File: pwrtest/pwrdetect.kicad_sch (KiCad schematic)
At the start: 37 parts, among them Q2 BC847, Q3 BC847, Q4 BC847, Q5 BC847, Q6 BC857, U10 TL431, U6 TL431DBZ, U7 TL431DBZ, U8 TL431DBZ, U9 TL431

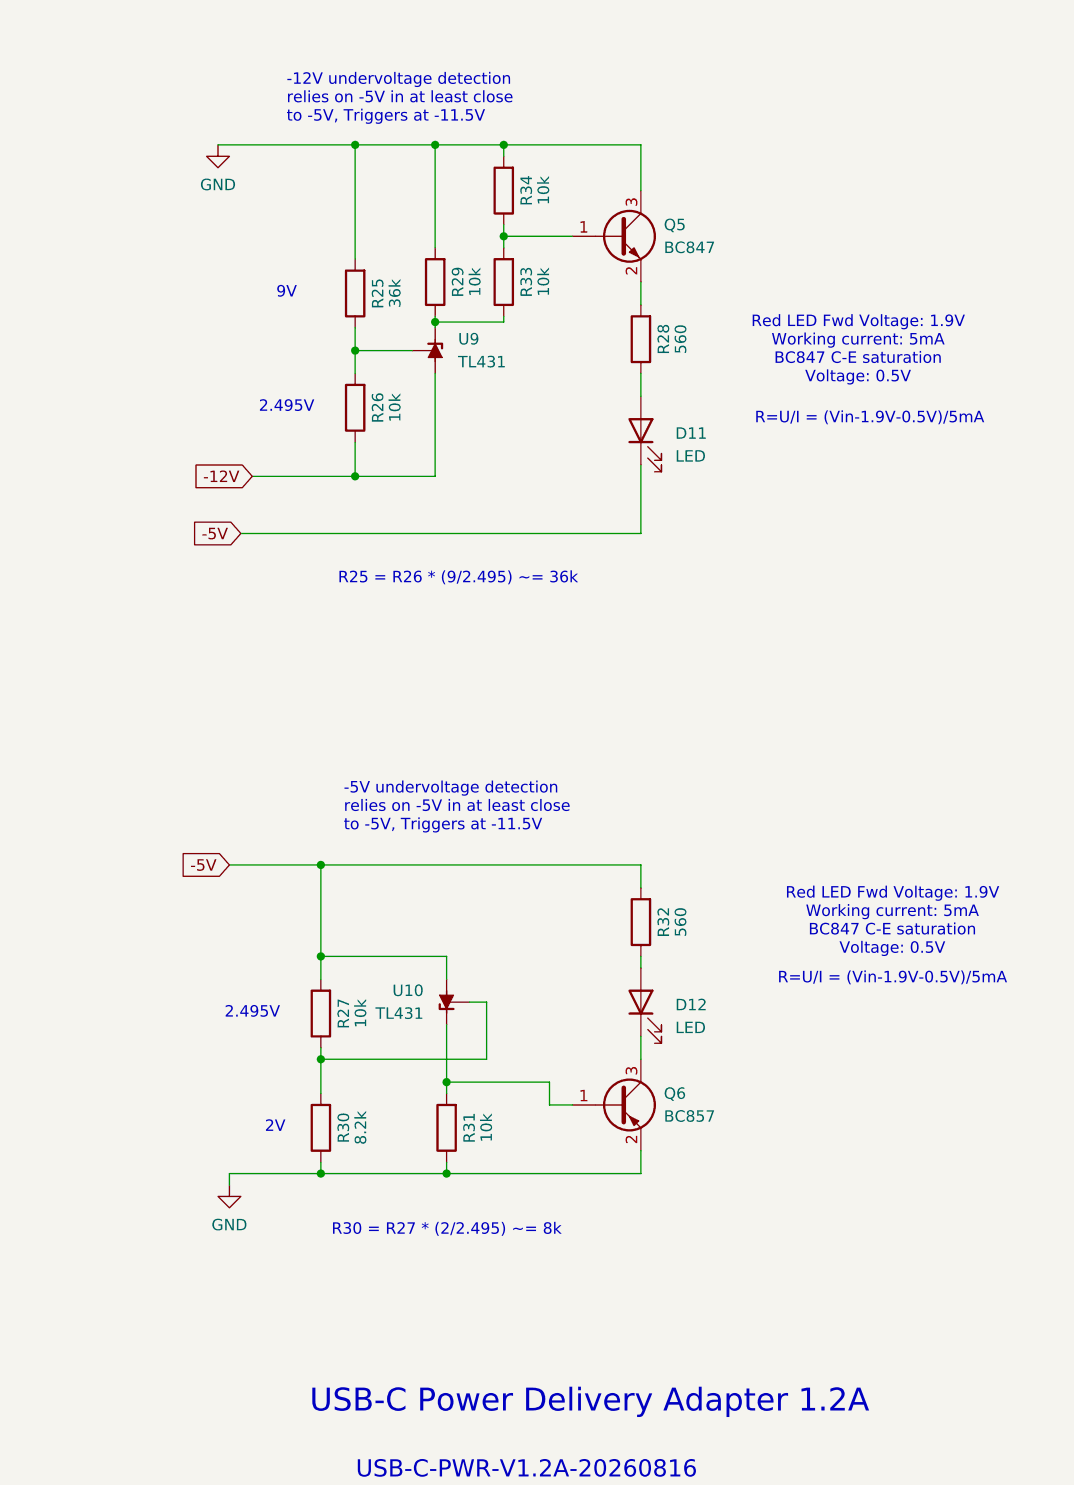
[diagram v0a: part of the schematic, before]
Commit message: new pwr adapter layout
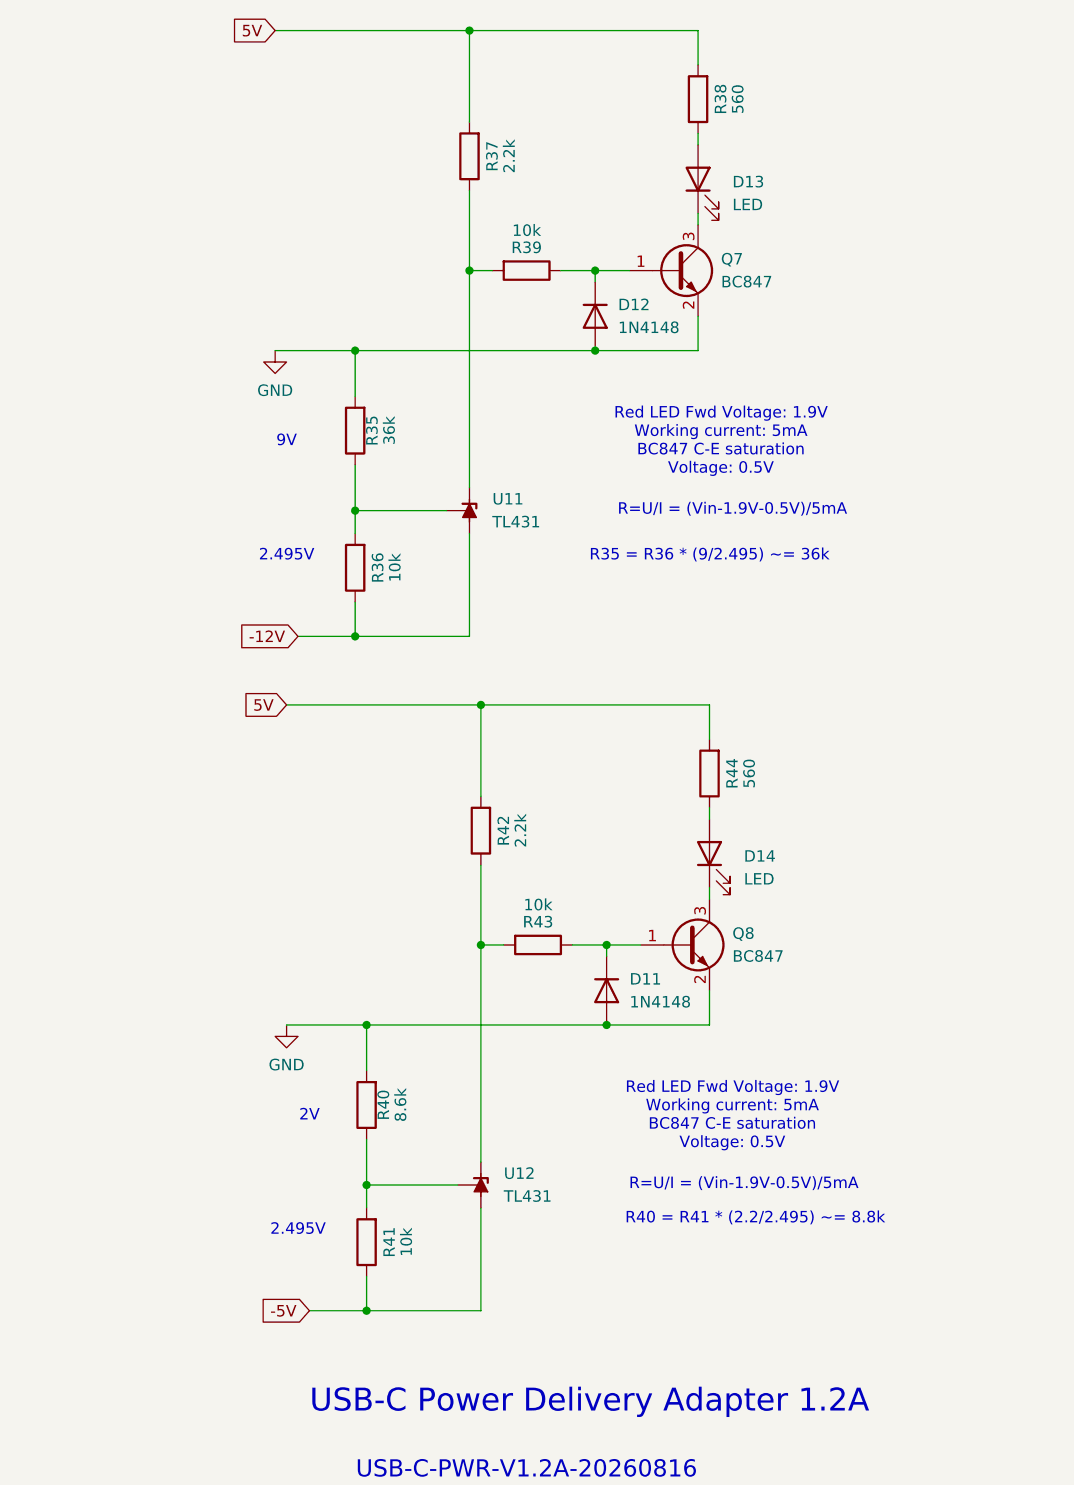
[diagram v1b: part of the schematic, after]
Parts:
- removed D11, D12: LED, Diode_SMD:D_0603_1608Metric_Pad1.05x0.95mm_HandSolder, symbol Device:LED
- removed Q5: BC847, Package_TO_SOT_SMD:SOT-23, symbol Transistor_BJT:BC847
- removed Q6: BC857, Package_TO_SOT_SMD:SOT-23, symbol Transistor_BJT:BC857
- removed R25: 36k, Resistor_SMD:R_0603_1608Metric_Pad0.98x0.95mm_HandSolder, symbol Device:R
- removed R26, R27, R29, R31, R33, R34: 10k, Resistor_SMD:R_0603_1608Metric_Pad0.98x0.95mm_HandSolder, symbol Device:R
- removed R28, R32: 560, Resistor_SMD:R_0603_1608Metric_Pad0.98x0.95mm_HandSolder, symbol Device:R
- removed R30: 8.2k, Resistor_SMD:R_0603_1608Metric_Pad0.98x0.95mm_HandSolder, symbol Device:R
- removed U10, U9: TL431, Package_TO_SOT_SMD:SOT-23, symbol Reference_Voltage:TL431DBZ
- added D11, D12: 1N4148, Diode_SMD:D_SOD-323_HandSoldering, symbol Diode:1N4148
- added D13, D14: LED, Diode_SMD:D_0603_1608Metric_Pad1.05x0.95mm_HandSolder, symbol Device:LED
- added Q7, Q8: BC847, Package_TO_SOT_SMD:SOT-23, symbol Transistor_BJT:BC847
- added R35: 36k, Resistor_SMD:R_0603_1608Metric_Pad0.98x0.95mm_HandSolder, symbol Device:R
- added R36, R39, R41, R43: 10k, Resistor_SMD:R_0603_1608Metric_Pad0.98x0.95mm_HandSolder, symbol Device:R
- added R37, R42: 2.2k, Resistor_SMD:R_0603_1608Metric_Pad0.98x0.95mm_HandSolder, symbol Device:R
- added R38, R44: 560, Resistor_SMD:R_0603_1608Metric_Pad0.98x0.95mm_HandSolder, symbol Device:R
- added R40: 8.6k, Resistor_SMD:R_0603_1608Metric_Pad0.98x0.95mm_HandSolder, symbol Device:R
- added U11, U12: TL431, Package_TO_SOT_SMD:SOT-23, symbol Reference_Voltage:TL431DBZ
- Q2, Q3, Q4: LCSC (none) -> C7420337
- R11: LCSC (none) -> C23147
- R14, R15, R18, R19, R22, R23: LCSC (none) -> C25804
- R16, R20, R24: LCSC (none) -> C23204
- R17: LCSC (none) -> C25819
- R21: LCSC (none) -> C25981
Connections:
- net -12V: now also R36.1, U11.3 (A)
- net -5V: now also R41.1, U12.3 (A)
- net 5V: now also R37.2, R38.2, R42.2, R44.2
- net GND: now also D11.2 (A), D12.2 (A), Q7.2 (E), Q8.2 (E), R35.2, R40.2
- new net: R42.1, R43.2, U12.1 (K)
- new net: R40.1, R41.2, U12.2 (REF)
- new net: D11.1 (K), Q8.1 (B), R43.1
- new net: D14.1 (K), Q8.3 (C)
- new net: D14.2 (A), R44.1
- new net: R37.1, R39.2, U11.1 (K)
- new net: R35.1, R36.2, U11.2 (REF)
- new net: D12.1 (K), Q7.1 (B), R39.1
- new net: D13.1 (K), Q7.3 (C)
- new net: D13.2 (A), R38.1
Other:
- note added: "R35 = R36 * (9/2.495) ~= 36k"
- note added: "R40 = R41 * (2.2/2.495) ~= 8.8k"
- note removed: "-12V undervoltage detection relies on -5V in at least close to -5V, Triggers at -11.5V"
- note removed: "-5V undervoltage detection relies on -5V in at least close to -5V, Triggers at -11.5V"
- note removed: "R25 = R26 * (9/2.495) ~= 36k"
- note removed: "R30 = R27 * (2/2.495) ~= 8k"

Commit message: add 0V in main pwr outputs
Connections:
- net 5V: no longer R19.2, R20.2
- new net 5VP: R19.2, R20.2
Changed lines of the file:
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@@
 		)
 	)
-	(global_label "5V"
+	(global_label "5VP"
 		(shape input)
 		(at 52.07 90.17 180)
@@
 		)
 		(property "Intersheetrefs" "${INTERSHEET_REFS}"
-			(at 46.7867 90.17 0)
+			(at 45.5167 90.17 0)
 			(hide yes)
 			(show_name no)
@@
 		(property "LCSC" "C7420337"
 			(at 100.33 115.5699 0)
+			(hide yes)
+			(show_name no)
+			(do_not_autoplace no)
 			(effects
 				(font
 					(size 1.27 1.27)
 				)
-				(hide yes)
 			)
 		)
@@
 		(property "LCSC" "C7420337"
 			(at 99.06 176.5299 0)
+			(hide yes)
+			(show_name no)
+			(do_not_autoplace no)
 			(effects
 				(font
 					(size 1.27 1.27)
 				)
-				(hide yes)
 			)
 		)
@@
 		(property "LCSC" "C7420337"
 			(at 233.68 118.1099 0)
+			(hide yes)
+			(show_name no)
+			(do_not_autoplace no)
 			(effects
 				(font
 					(size 1.27 1.27)
 				)
-				(hide yes)
 			)
 		)
@@
 		(property "LCSC" "C7420337"
 			(at 232.41 43.1799 0)
+			(hide yes)
+			(show_name no)
+			(do_not_autoplace no)
 			(effects
 				(font
 					(size 1.27 1.27)
 				)
-				(hide yes)
 			)
 		)
@@
 		(property "LCSC" "C7420337"
 			(at 97.79 55.8799 0)
+			(hide yes)
+			(show_name no)
+			(do_not_autoplace no)
 			(effects
 				(font
 					(size 1.27 1.27)
 				)
-				(hide yes)
 			)
 		)

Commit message: add note for broken TL431 layout
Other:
- note added: "NOTE: ALL TL431 have REF and Cathode swapped in pinout!"
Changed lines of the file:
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@@
+		)
+	)
+	(text "NOTE:\nALL TL431 have \nREF and Cathode\nswapped in pinout!"
+		(exclude_from_sim no)
+		(at 144.78 64.77 0)
+		(effects
+			(font
+				(size 4.445 4.445)
+				(thickness 0.889)
+				(bold yes)
+				(color 255 0 45 1)
+			)
 		)
 	)

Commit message: note on tl431 circuits
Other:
- note added: "All the pos voltage comparators (5V, 12V, Vbus) won't work as the TL431 pulls to 2V only. Requires an PNP setup instead."
- note added: "Also, TL431 needs at approx 1mA Ika to regulate"
- note added: "NOTE: ALL TL431 have REF and Cathode swapped in pinout as the BOM part is a TL431A-MS"
- note removed: "NOTE: ALL TL431 have REF and Cathode swapped in pinout!"
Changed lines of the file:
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@@
 		)
 	)
-	(text "NOTE:\nALL TL431 have \nREF and Cathode\nswapped in pinout!"
+	(text "NOTE:\nALL TL431 have \nREF and Cathode\nswapped in pinout\nas the BOM part\nis a TL431A-MS"
 		(exclude_from_sim no)
-		(at 144.78 64.77 0)
+		(at 143.51 67.564 0)
 		(effects
 			(font
-				(size 4.445 4.445)
+				(size 3.175 3.175)
 				(thickness 0.889)
 				(bold yes)
@@
 		)
 	)
+	(text "Also, TL431 needs\nat approx 1mA Ika\nto regulate"
+		(exclude_from_sim no)
+		(at 140.716 178.308 0)
+		(effects
+			(font
+				(size 3.175 3.175)
+				(thickness 0.889)
+				(bold yes)
+				(color 255 0 45 1)
+			)
+		)
+	)
 	(text "Red LED Fwd Voltage: 1.9V\nWorking current: 5mA\nBC847 C-E saturation \nVoltage: 0.5V"
 		(exclude_from_sim no)
@@
 			)
 		)
+	)
+	(text "All the pos voltage \ncomparators (5V, 12V, Vbus)\nwon't work\nas the TL431 pulls to \n2V only. Requires an\nPNP setup instead."
+		(exclude_from_sim no)
+		(at 142.748 127.762 0)
+		(effects
+			(font
+				(size 3.175 3.175)
+				(thickness 0.889)
+				(bold yes)
+				(color 255 0 45 1)
+			)
+		)

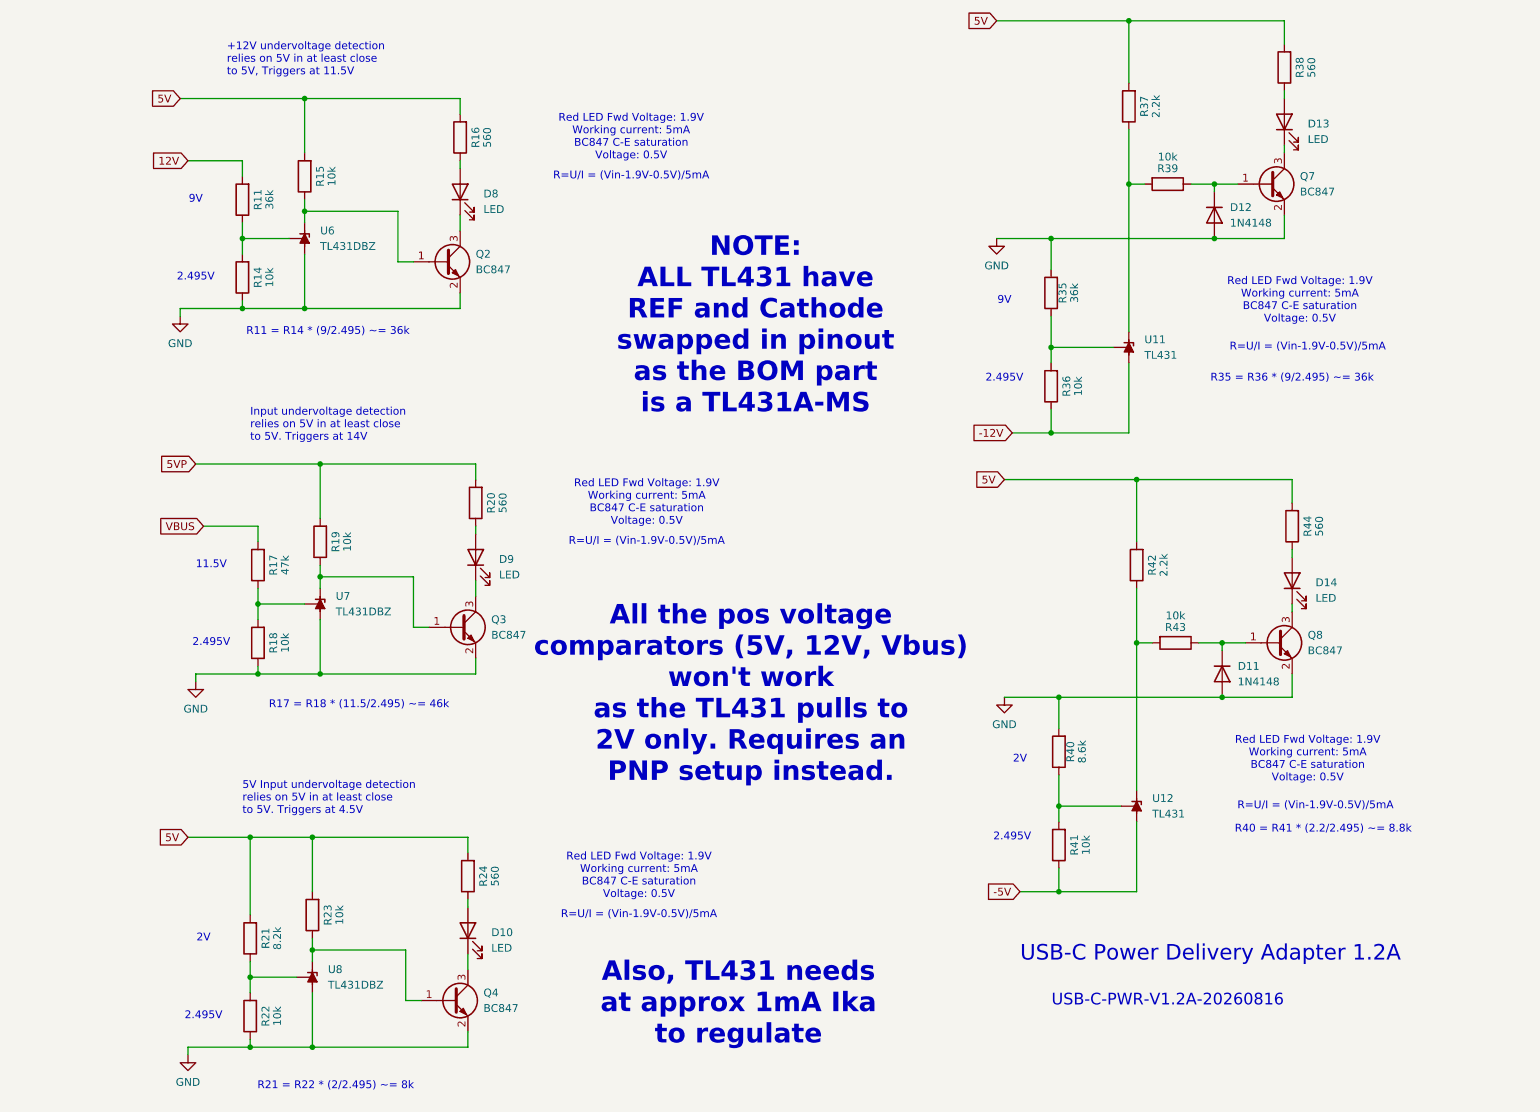
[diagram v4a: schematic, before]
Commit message: updated schematics (untested)
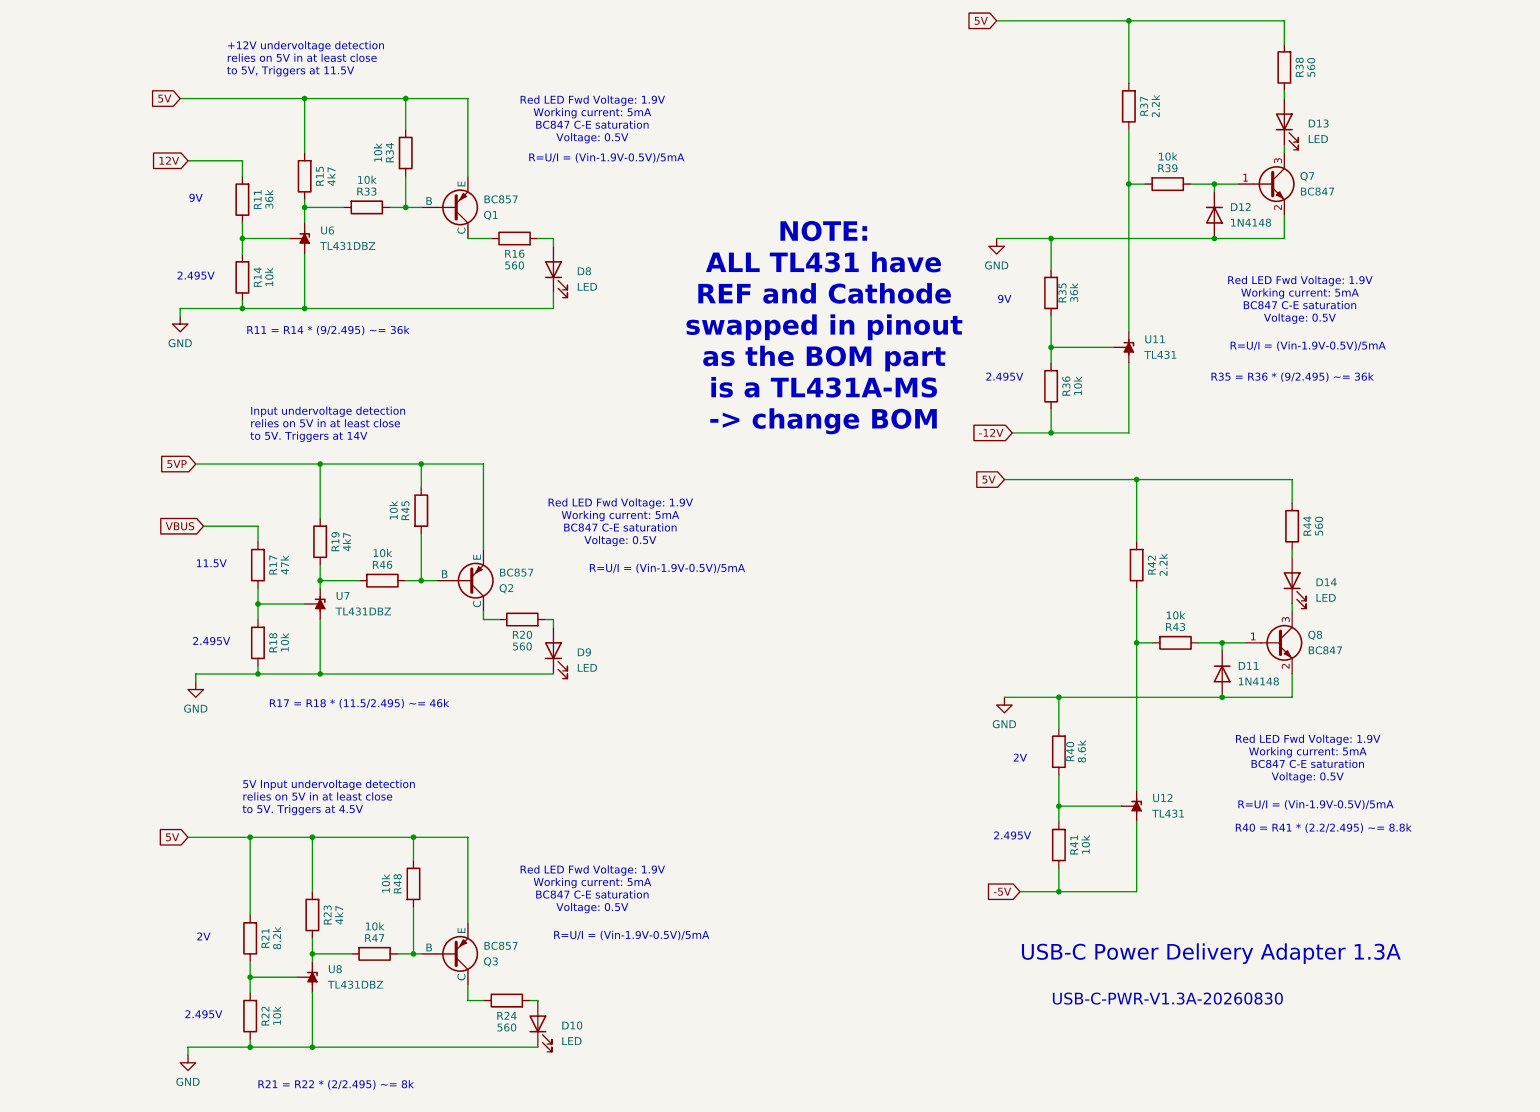
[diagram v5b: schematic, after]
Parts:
- removed Q2, Q3, Q4: BC847, Package_TO_SOT_SMD:SOT-23, symbol Transistor_BJT:BC847
- added Q1, Q2, Q3: BC857, Package_TO_SOT_SMD:SOT-23, symbol Simulation_SPICE:PNP
- added R33, R34, R45, R46, R47, R48: 10k, Resistor_SMD:R_0603_1608Metric_Pad0.98x0.95mm_HandSolder, symbol Device:R
- R15, R19, R23: value 10k -> 4k7; LCSC C25804 -> (none)
- U11, U12, U6, U7, U8: LCSC C19272793 -> (none)
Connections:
- net 5V: now also Q1.3 (E), Q3.3 (E), R34.1, R48.1; no longer R16.2, R24.2
- net 5VP: now also Q2.3 (E), R45.1; no longer R20.2
- net GND: now also D10.1 (K), D8.1 (K), D9.1 (K)
- net at R23.1, U8.1 (K): now also R47.2
- net at R19.1, U7.1 (K): now also R46.2
- net at D8.2 (A): now also R16.2; no longer R16.1
- net at R15.1, U6.1 (K): now also R33.2
- net at D10.2 (A): now also R24.2; no longer R24.1
- net at R20.1: now also Q2.1 (C); no longer D9.2 (A)
- new net: Q2.2 (B), R45.2, R46.1
- new net: Q3.2 (B), R47.1, R48.2
- new net: Q1.2 (B), R33.1, R34.2
- new net: Q3.1 (C), R24.1
- new net: Q1.1 (C), R16.1
- new net: D9.2 (A), R20.2
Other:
- note added: "NOTE: ALL TL431 have REF and Cathode swapped in pinout as the BOM part is a TL431A-MS -> change BOM"
- note added: "USB-C Power Delivery Adapter 1.3A"
- note added: "USB-C-PWR-V1.3A-20260830"
- note removed: "All the pos voltage comparators (5V, 12V, Vbus) won't work as the TL431 pulls to 2V only. Requires an PNP setup instead."
- note removed: "Also, TL431 needs at approx 1mA Ika to regulate"
- note removed: "NOTE: ALL TL431 have REF and Cathode swapped in pinout as the BOM part is a TL431A-MS"
- note removed: "USB-C Power Delivery Adapter 1.2A"
- note removed: "USB-C-PWR-V1.2A-20260816"
- moved on the sheet: D10, D8, D9, R16, R20, R24

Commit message: usb pd updated
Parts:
- removed R15, R19, R23: 4k7, Resistor_SMD:R_0603_1608Metric_Pad0.98x0.95mm_HandSolder, symbol Device:R
- R16, R20, R24: value 560 -> 680; LCSC C23204 -> (none)
- R33, R34, R45, R46, R47, R48: value 10k -> 2k2; LCSC C25804 -> (none)
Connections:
- net 5V: now also D10.2 (A), D8.2 (A)
- net 5VP: now also D9.2 (A)
- net GND: now also R16.2, R20.2, R24.2; no longer D10.1 (K), D8.1 (K), D9.1 (K)
- net at Q2.1 (C), R20.1: now also D9.1 (K)
- net at Q3.1 (C), R24.1: now also D10.1 (K)
- net at Q1.1 (C), R16.1: now also D8.1 (K)
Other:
- note added: "1.3B: - fix brownout detection for positive voltages"
- note added: "NOTE: There are TL431 variants with REF and Cathode swapped in pinout. Watch out in parts selection!"
- note added: "R=U/I = (Vin-1.9V)/5mA"
- note added: "USB-C Power Delivery Adapter 1.3B"
- note added: "USB-C-PWR-V1.3B-20260905"
- note removed: "NOTE: ALL TL431 have REF and Cathode swapped in pinout as the BOM part is a TL431A-MS -> change BOM"
- note removed: "USB-C Power Delivery Adapter 1.3A"
- note removed: "USB-C-PWR-V1.3A-20260830"
- moved on the sheet: D10, D8, D9, R16, R20, R24
